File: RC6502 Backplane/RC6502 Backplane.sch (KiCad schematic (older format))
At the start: 16 parts, among them J1 RC6502_Backplane, J2 Barrel_Jack, J3 RC6502_Backplane, J4 RC6502_Backplane, J5 RC6502_Backplane, J6 RC6502_Backplane, U1 LM7805

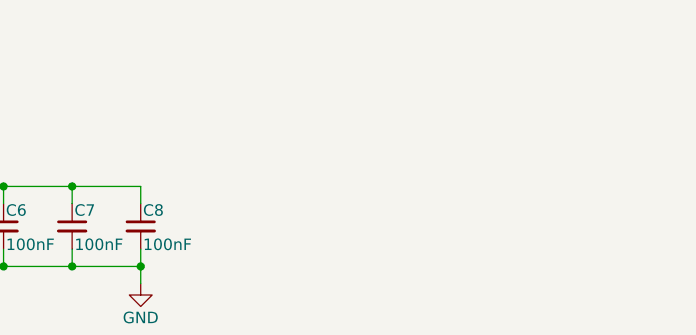
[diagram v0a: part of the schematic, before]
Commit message: Backplane layout done
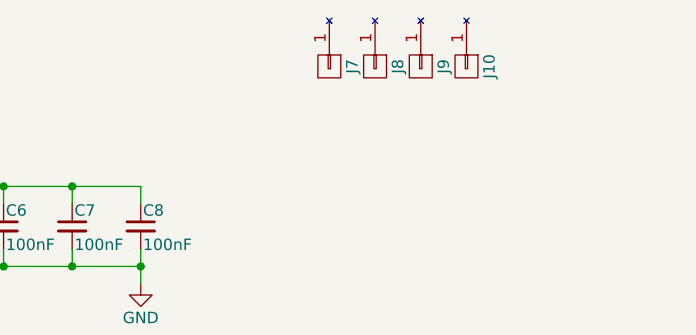
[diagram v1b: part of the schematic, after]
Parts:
- added J10, J7, J8, J9: Mounting, mounting:Mounting, symbol Mounting
- C1: footprint (none) -> Capacitors_THT:CP_Radial_D5.0mm_P2.50mm
- C2: footprint (none) -> Capacitors_THT:CP_Radial_D4.0mm_P2.00mm
- C3, C4, C5, C6, C7, C8: footprint (none) -> Capacitors_THT:C_Disc_D4.7mm_W2.5mm_P5.00mm
- J1, J3, J4, J5, J6: footprint (none) -> Pin_Headers:Pin_Header_Straight_1x39_Pitch2.54mm
- J2: footprint (none) -> Connectors:BARREL_JACK
- JP1: footprint (none) -> Pin_Headers:Pin_Header_Straight_1x02_Pitch2.54mm
- U1: footprint TO_SOT_Packages_THT:TO-220_Vertical -> TO_SOT_Packages_THT:TO-220-3_Horizontal
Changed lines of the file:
@@
 LIBS:valves
 LIBS:rc6502_backplane
+LIBS:mounting
+LIBS:RC6502 Backplane-cache
 EELAYER 25 0
 EELAYER END
@@
 F 0 "J6" H 10425 6375 50  0000 C CNN
 F 1 "RC6502_Backplane" V 10875 4325 50  0000 C CNN
-F 2 "" H 10425 4375 50  0001 C CNN
+F 2 "Pin_Headers:Pin_Header_Straight_1x39_Pitch2.54mm" H 10425 4375 50  0001 C CNN
 F 3 "" H 10425 4375 50  0001 C CNN
 	1    10425 4375
@@
 F 0 "C4" H 8235 1545 50  0000 L CNN
 F 1 "100nF" H 8235 1395 50  0000 L CNN
-F 2 "" H 8225 1475 50  0001 C CNN
+F 2 "Capacitors_THT:C_Disc_D4.7mm_W2.5mm_P5.00mm" H 8225 1475 50  0001 C CNN
 F 3 "" H 8225 1475 50  0001 C CNN
 	1    8225 1475
@@
 F 0 "C5" H 8535 1545 50  0000 L CNN
 F 1 "100nF" H 8535 1395 50  0000 L CNN
-F 2 "" H 8525 1475 50  0001 C CNN
+F 2 "Capacitors_THT:C_Disc_D4.7mm_W2.5mm_P5.00mm" H 8525 1475 50  0001 C CNN
 F 3 "" H 8525 1475 50  0001 C CNN
 	1    8525 1475
@@
 F 0 "C6" H 8835 1545 50  0000 L CNN
 F 1 "100nF" H 8835 1395 50  0000 L CNN
-F 2 "" H 8825 1475 50  0001 C CNN
+F 2 "Capacitors_THT:C_Disc_D4.7mm_W2.5mm_P5.00mm" H 8825 1475 50  0001 C CNN
 F 3 "" H 8825 1475 50  0001 C CNN
 	1    8825 1475
@@
 F 0 "C7" H 9135 1545 50  0000 L CNN
 F 1 "100nF" H 9135 1395 50  0000 L CNN
-F 2 "" H 9125 1475 50  0001 C CNN
+F 2 "Capacitors_THT:C_Disc_D4.7mm_W2.5mm_P5.00mm" H 9125 1475 50  0001 C CNN
 F 3 "" H 9125 1475 50  0001 C CNN
 	1    9125 1475
@@
 F 0 "C8" H 9435 1545 50  0000 L CNN
 F 1 "100nF" H 9435 1395 50  0000 L CNN
-F 2 "" H 9425 1475 50  0001 C CNN
+F 2 "Capacitors_THT:C_Disc_D4.7mm_W2.5mm_P5.00mm" H 9425 1475 50  0001 C CNN
 F 3 "" H 9425 1475 50  0001 C CNN
 	1    9425 1475
@@
 F 0 "C3" H 6110 1570 50  0000 L CNN
 F 1 "100nF" H 6110 1420 50  0000 L CNN
-F 2 "" H 6100 1500 50  0001 C CNN
+F 2 "Capacitors_THT:C_Disc_D4.7mm_W2.5mm_P5.00mm" H 6100 1500 50  0001 C CNN
 F 3 "" H 6100 1500 50  0001 C CNN
 	1    6100 1500
@@
 F 0 "J5" H 8600 6375 50  0000 C CNN
 F 1 "RC6502_Backplane" V 9050 4325 50  0000 C CNN
-F 2 "" H 8600 4375 50  0001 C CNN
+F 2 "Pin_Headers:Pin_Header_Straight_1x39_Pitch2.54mm" H 8600 4375 50  0001 C CNN
 F 3 "" H 8600 4375 50  0001 C CNN
 	1    8600 4375
@@
 F 0 "J4" H 6650 6375 50  0000 C CNN
 F 1 "RC6502_Backplane" V 7100 4325 50  0000 C CNN
-F 2 "" H 6650 4375 50  0001 C CNN
+F 2 "Pin_Headers:Pin_Header_Straight_1x39_Pitch2.54mm" H 6650 4375 50  0001 C CNN
 F 3 "" H 6650 4375 50  0001 C CNN
 	1    6650 4375
@@
 F 0 "J3" H 4825 6375 50  0000 C CNN
 F 1 "RC6502_Backplane" V 5275 4325 50  0000 C CNN
-F 2 "" H 4825 4375 50  0001 C CNN
+F 2 "Pin_Headers:Pin_Header_Straight_1x39_Pitch2.54mm" H 4825 4375 50  0001 C CNN
 F 3 "" H 4825 4375 50  0001 C CNN
 	1    4825 4375
@@
 F 0 "J1" H 2875 6375 50  0000 C CNN
 F 1 "RC6502_Backplane" V 3325 4325 50  0000 C CNN
-F 2 "" H 2875 4375 50  0001 C CNN
+F 2 "Pin_Headers:Pin_Header_Straight_1x39_Pitch2.54mm" H 2875 4375 50  0001 C CNN
 F 3 "" H 2875 4375 50  0001 C CNN
 	1    2875 4375
@@
 F 0 "J2" H 4450 1610 50  0000 C CNN
 F 1 "Barrel_Jack" H 4450 1225 50  0000 C CNN
-F 2 "" H 4500 1360 50  0001 C CNN
+F 2 "Connectors:BARREL_JACK" H 4500 1360 50  0001 C CNN
 F 3 "" H 4500 1360 50  0001 C CNN
 	1    4450 1400
@@
 F 0 "U1" H 5300 1425 50  0000 C CNN
 F 1 "LM7805" H 5450 1425 50  0000 L CNN
-F 2 "TO_SOT_Packages_THT:TO-220_Vertical" H 5450 1525 50  0001 C CIN
+F 2 "TO_SOT_Packages_THT:TO-220-3_Horizontal" H 5450 1525 50  0001 C CIN
 F 3 "" H 5450 1250 50  0001 C CNN
 	1    5450 1300
@@
 F 0 "JP1" H 5450 1055 50  0000 C CNN
 F 1 "NO_REG" H 5460 915 50  0000 C CNN
-F 2 "" H 5450 975 50  0001 C CNN
+F 2 "Pin_Headers:Pin_Header_Straight_1x02_Pitch2.54mm" H 5450 975 50  0001 C CNN
 F 3 "" H 5450 975 50  0001 C CNN
 	1    5450 975
@@
 F 0 "C1" H 5085 1570 50  0000 L CNN
 F 1 "100uF" H 5085 1420 50  0000 L CNN
-F 2 "" H 5075 1500 50  0001 C CNN
+F 2 "Capacitors_THT:CP_Radial_D5.0mm_P2.50mm" H 5075 1500 50  0001 C CNN
 F 3 "" H 5075 1500 50  0001 C CNN
 	1    5075 1500
@@
 F 0 "C2" H 5835 1570 50  0000 L CNN
 F 1 "10uF" H 5835 1420 50  0000 L CNN
-F 2 "" H 5825 1500 50  0001 C CNN
+F 2 "Capacitors_THT:CP_Radial_D4.0mm_P2.00mm" H 5825 1500 50  0001 C CNN
 F 3 "" H 5825 1500 50  0001 C CNN
 	1    5825 1500
@@
 	1    0    0    -1
 $EndComp
+$Comp
+L Mounting J7
+U 1 1 5C334F92
+P 10250 775
+F 0 "J7" H 10250 875 50  0000 C CNN
+F 1 "Mounting" V 10350 775 50  0001 C CNN
+F 2 "mounting:Mounting" H 10250 775 50  0001 C CNN
+F 3 "" H 10250 775 50  0001 C CNN
+	1    10250 775
+	0    1    1    0
+$EndComp
+$Comp
+L Mounting J8
+U 1 1 5C3350AD
+P 10450 775
+F 0 "J8" H 10450 875 50  0000 C CNN
+F 1 "Mounting" V 10550 775 50  0001 C CNN
+F 2 "mounting:Mounting" H 10450 775 50  0001 C CNN
+F 3 "" H 10450 775 50  0001 C CNN
+	1    10450 775
+	0    1    1    0
+$EndComp
+$Comp
+L Mounting J9
+U 1 1 5C3350FF
+P 10650 775
+F 0 "J9" H 10650 875 50  0000 C CNN
+F 1 "Mounting" V 10750 775 50  0001 C CNN
+F 2 "mounting:Mounting" H 10650 775 50  0001 C CNN
+F 3 "" H 10650 775 50  0001 C CNN
+	1    10650 775
+	0    1    1    0
+$EndComp
+$Comp
+L Mounting J10
+U 1 1 5C33514E
+P 10850 775
+F 0 "J10" H 10850 875 50  0000 C CNN
+F 1 "Mounting" V 10950 775 50  0001 C CNN
+F 2 "mounting:Mounting" H 10850 775 50  0001 C CNN
+F 3 "" H 10850 775 50  0001 C CNN
+	1    10850 775
+	0    1    1    0
+$EndComp
 $EndSCHEMATC

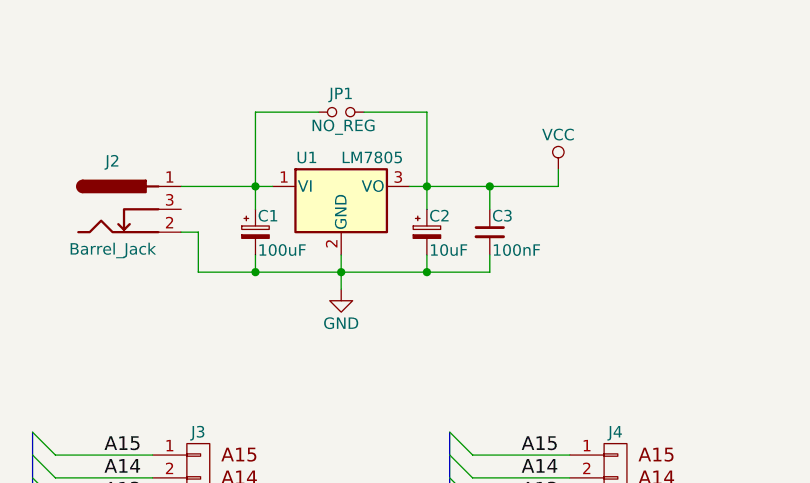
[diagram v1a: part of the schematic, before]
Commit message: Added bleed LED to backplane
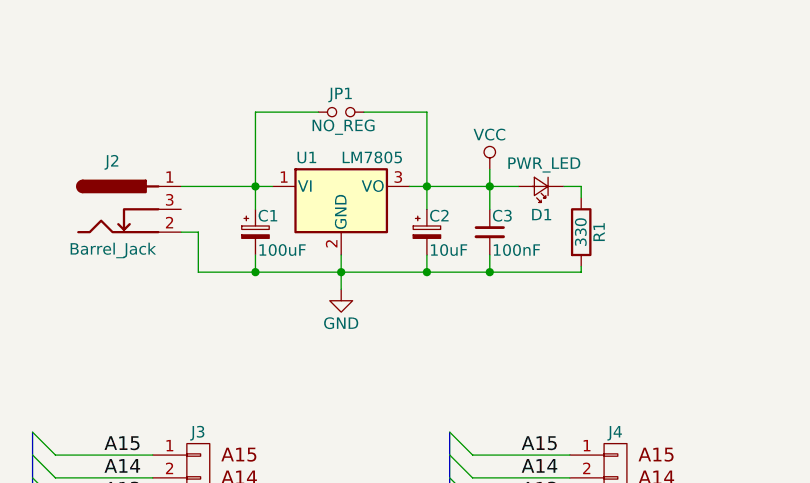
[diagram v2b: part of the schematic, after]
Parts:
- added D1: PWR_LED, LEDs:LED_D5.0mm, symbol LED_Small
- added R1: 330, Resistors_THT:R_Axial_DIN0207_L6.3mm_D2.5mm_P10.16mm_Horizontal, symbol R
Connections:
- net GND: now also R1.2
- net VCC: now also D1.2 (A)
- new net: D1.1 (K), R1.1
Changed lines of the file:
@@
 	5075 975  5350 975
 Wire Wire Line
-	5750 1300 6400 1300
+	5750 1300 6225 1300
 Wire Wire Line
 	5825 975  5825 1400
@@
 	5075 1600 5075 1675
 Wire Wire Line
-	4825 1675 6100 1675
+	4825 1675 6500 1675
 Wire Wire Line
 	5450 1600 5450 1750
@@
 Connection ~ 5825 1300
 Wire Wire Line
-	6100 1300 6100 1400
-Wire Wire Line
-	6400 1300 6400 1225
+	6100 1225 6100 1400
 Connection ~ 6100 1300
 $Comp
 L VCC #PWR013
 U 1 1 5C2F8202
-P 6400 1225
-F 0 "#PWR013" H 6400 1075 50  0001 C CNN
-F 1 "VCC" H 6400 1375 50  0000 C CNN
-F 2 "" H 6400 1225 50  0001 C CNN
-F 3 "" H 6400 1225 50  0001 C CNN
-	1    6400 1225
+P 6100 1225
+F 0 "#PWR013" H 6100 1075 50  0001 C CNN
+F 1 "VCC" H 6100 1375 50  0000 C CNN
+F 2 "" H 6100 1225 50  0001 C CNN
+F 3 "" H 6100 1225 50  0001 C CNN
+	1    6100 1225
 	1    0    0    -1
 $EndComp
@@
 	0    1    1    0
 $EndComp
+$Comp
+L LED_Small D1
+U 1 1 5C61CD3B
+P 6325 1300
+F 0 "D1" H 6275 1425 50  0000 L CNN
+F 1 "PWR_LED" H 6150 1200 50  0000 L CNN
+F 2 "LEDs:LED_D5.0mm" V 6325 1300 50  0001 C CNN
+F 3 "" V 6325 1300 50  0001 C CNN
+	1    6325 1300
+	-1   0    0    1
+$EndComp
+Wire Wire Line
+	6425 1300 6500 1300
+$Comp
+L R R1
+U 1 1 5C61D653
+P 6500 1500
+F 0 "R1" V 6580 1500 50  0000 C CNN
+F 1 "330" V 6500 1500 50  0000 C CNN
+F 2 "Resistors_THT:R_Axial_DIN0207_L6.3mm_D2.5mm_P10.16mm_Horizontal" V 6430 1500 50  0001 C CNN
+F 3 "" H 6500 1500 50  0001 C CNN
+	1    6500 1500
+	1    0    0    -1
+$EndComp
+Wire Wire Line
+	6500 1300 6500 1350
+Connection ~ 6100 1675
+Wire Wire Line
+	6500 1675 6500 1650
 $EndSCHEMATC
